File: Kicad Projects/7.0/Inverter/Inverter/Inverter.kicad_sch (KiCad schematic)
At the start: 75 parts, among them IC1 1ED3322MC12NXUMA1, IC2 B0505S-2W, IC3 B0505S-2W, IC4 B0505S-2W, IC5 1ED3322MC12NXUMA1, J1 Conn_01x02_Male, J2 Conn_01x07_Male, J3 Conn_01x02_Male, U1 LM7809_TO220, U2 LM7809_TO220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

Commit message: Inverter PCB Done
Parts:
- removed C29: 56uF, Capacitor_THT:CP_Radial_D16.0mm_P7.50mm, symbol Device:C_Polarized
- removed C3, C4: 1000uF, 25V 1000uf:CAP_EEEFK1E102AQ, symbol Device:C_Polarized
- added D10, D11, D9: Blue, LED_SMD:LED_0805_2012Metric_Pad1.15x1.40mm_HandSolder, symbol Device:LED
- added D12, D13: Red, LED_SMD:LED_0805_2012Metric_Pad1.15x1.40mm_HandSolder, symbol Device:LED
- added D14, D15, D16, D17, D18, D19: Green, LED_SMD:LED_0805_2012Metric_Pad1.15x1.40mm_HandSolder, symbol Device:LED
- added J4: Output Selector, Connector_PinSocket_1.27mm:PinSocket_1x03_P1.27mm_Vertical, symbol Connector:Conn_01x03_Pin
- added Q1, Q2: FS8205, 8205a:SOT95P280X145-6N, symbol 8205a:FS8205
- added R11, R12: 1.4, Resistor_SMD:R_0805_2012Metric_Pad1.20x1.40mm_HandSolder, symbol Device:R
- added R13, R14, R15, R16, R17: 22K, Resistor_SMD:R_1206_3216Metric_Pad1.30x1.75mm_HandSolder, symbol Device:R
- added R18, R19, R20, R21, R22, R27: 470, Resistor_SMD:R_0603_1608Metric_Pad0.98x0.95mm_HandSolder, symbol Device:R
- added R23, R26: 3.3k, Resistor_SMD:R_0603_1608Metric_Pad0.98x0.95mm_HandSolder, symbol Device:R
- added R24, R25: 2.2k, Resistor_SMD:R_0603_1608Metric_Pad0.98x0.95mm_HandSolder, symbol Device:R
- R1, R3: value 3.3 -> 2.2
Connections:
- net +BATT: now also R13.1, R16.1
- net -BATT: now also D18.1 (K); no longer R7.2
- net DIG+: now also J4.3 (Pin_3), R21.2, R22.2, R27.1
- net DIG-: now also D10.1 (K), D11.1 (K), D19.1 (K), D9.1 (K), Q1.1, Q1.3, Q2.1, Q2.3
- net DIG5V: now also J4.1 (Pin_1); no longer J2.2 (Pin_2)
- net FLT: now also Q1.4, Q1.6
- net GND1: now also D14.1 (K), R24.2
- net GND2: now also D16.1 (K), R25.2
- net INHS: now also R19.1
- net INLS: now also R18.1
- net RDY: now also Q2.4, Q2.6
- net RST: now also R20.1
- net VAux+: now also J3.2 (Pin_2); no longer J3.1 (Pin_1)
- net VAux-: now also J3.1 (Pin_1); no longer J3.2 (Pin_2)
- net VDrive1: now also R23.2
- net VDrive1Neg: now also D15.1 (K)
- net VDrive2: now also R26.2
- net VDrive2Neg: now also D17.1 (K)
- net at R3.2, U7.4: now also IC5.7 (CLAMP), R12.2
- net at R1.2, U7.6: now also IC1.7 (CLAMP), R11.2
- net at IC5.4 (OUT-): now also R12.1
- net at IC1.4 (OUT-): now also R11.1
- new net: D15.2 (A), R24.1
- new net: D17.2 (A), R25.1
- new net: R13.2, R14.1, R15.1, R16.2, R17.1, R7.2
- new net: J2.2 (Pin_2), J4.2 (Pin_2)
- new net: D13.1 (K), Q2.2, Q2.5
- new net: D12.2 (A), R21.1
- new net: D10.2 (A), R19.2
- new net: D9.2 (A), R18.2
- new net: D12.1 (K), Q1.2, Q1.5
- new net: D13.2 (A), R22.1
- new net: D16.2 (A), R26.1
- new net: D18.2 (A), R14.2, R15.2, R17.2
- new net: D19.2 (A), R27.2
- new net: D11.2 (A), R20.2
- new net: D14.2 (A), R23.1
- no-connect marks 2 -> 0
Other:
- moved on the sheet: R10, R8, R9

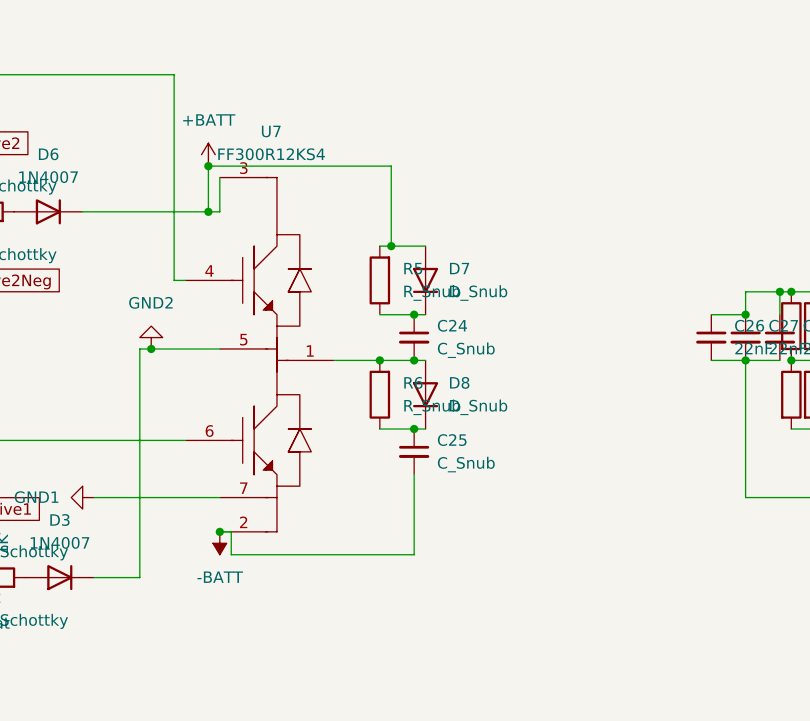
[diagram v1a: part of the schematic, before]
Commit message: IDEK but LTC6804 Ordered
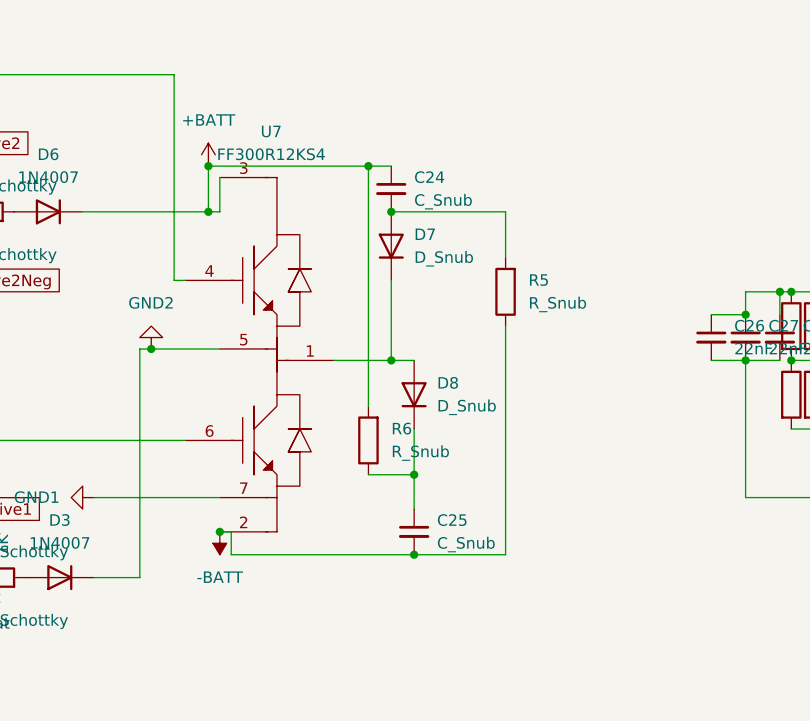
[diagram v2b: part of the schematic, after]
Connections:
- net +BATT: now also C24.1, R6.2; no longer D7.2 (A), R5.2
- net -BATT: now also R5.1
- net at D8.2 (A), U7.1: now also D7.1 (K); no longer C24.2, R6.2
- new net: C24.2, D7.2 (A), R5.2
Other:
- moved on the sheet: C24, C25, D7, D8, R5, R6

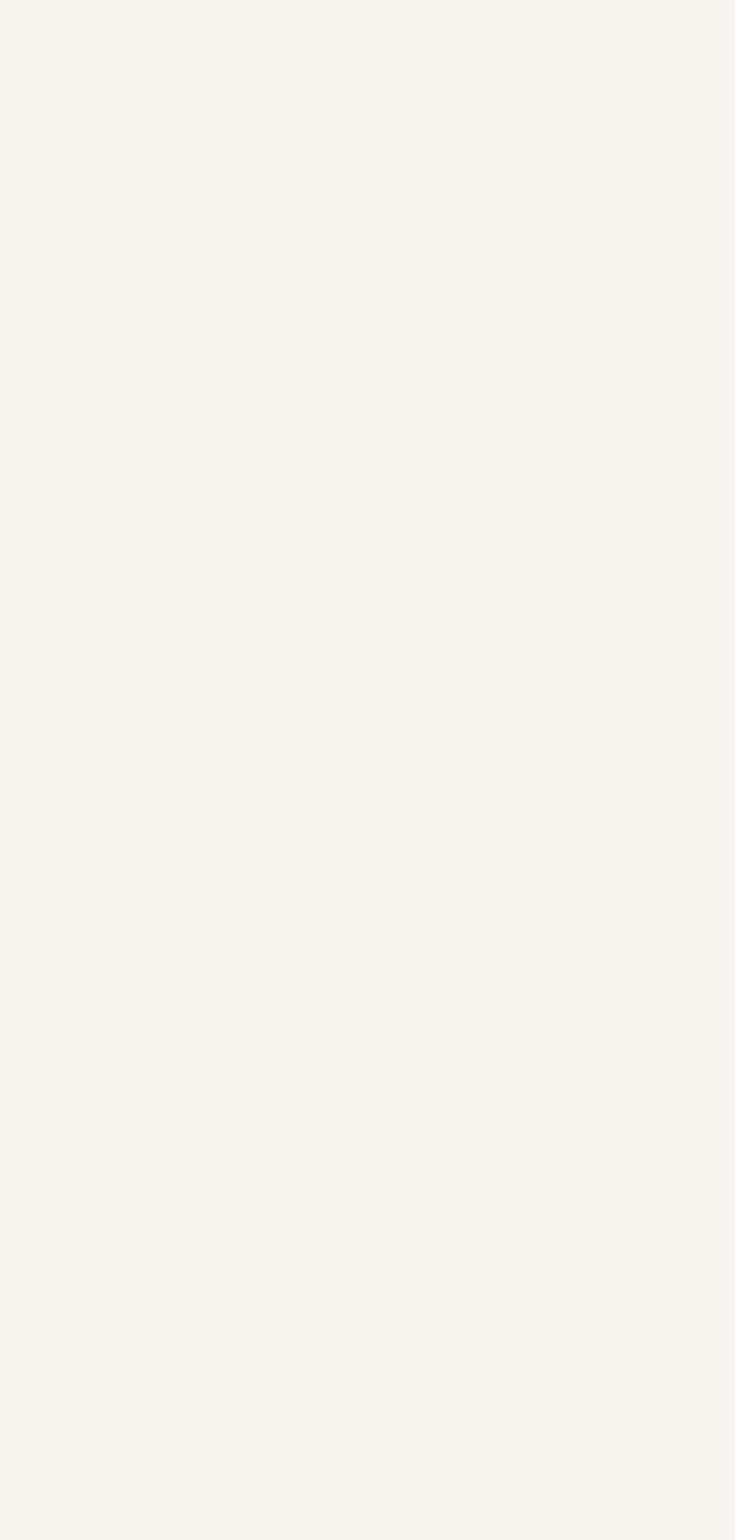
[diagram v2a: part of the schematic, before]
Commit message: Inverter 0 errors ready to export, LU fucked
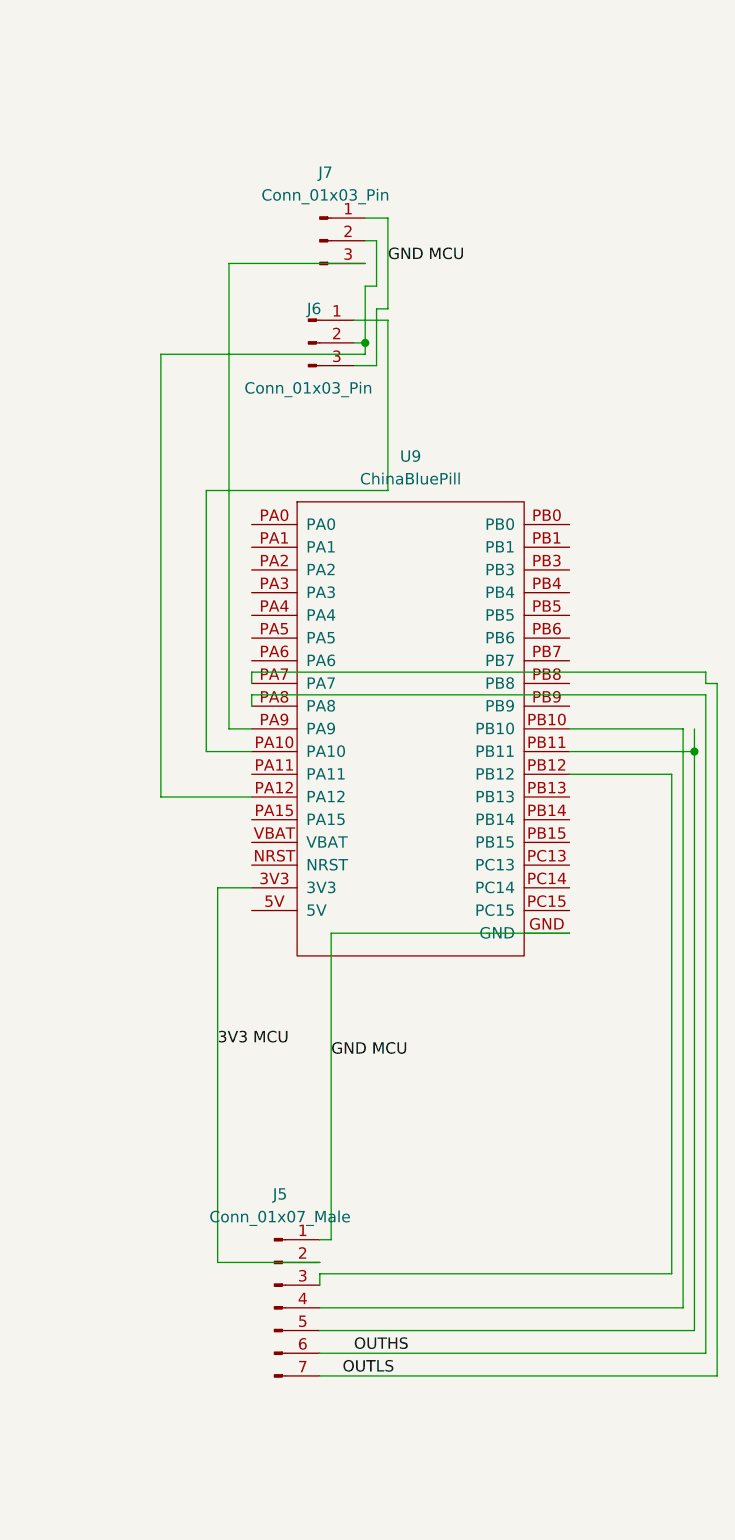
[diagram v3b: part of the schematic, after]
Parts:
- added J5: Conn_01x07_Male, Connector_JST:JST_XH_B7B-XH-A_1x07_P2.50mm_Vertical, symbol Connector:Conn_01x07_Male
- added J6, J7: Conn_01x03_Pin, Connector_JST:JST_XH_S3B-XH-A_1x03_P2.50mm_Horizontal, symbol Connector:Conn_01x03_Pin
- added U9: ChinaBluePill, Blue Pill:ChinaBluePill, symbol Blue Pill:ChinaBluePill
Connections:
- new net: J5.3 (Pin_3), U9.PB12
- new net: J5.4 (Pin_4), U9.PB10
- new net: J5.5 (Pin_5), U9.PB11
- new net: J6.2 (Pin_2), J7.2 (Pin_2), U9.PA12
- new net: J7.3 (Pin_3), U9.PA9
- new net: J6.1 (Pin_1), U9.PA10
- new net 3V3 MCU: J5.2 (Pin_2), U9.3V3
- new net GND MCU: J5.1 (Pin_1), J6.3 (Pin_3), J7.1 (Pin_1), U9.GND
- new net OUTHS: J5.6 (Pin_6), U9.PA8
- new net OUTLS: J5.7 (Pin_7), U9.PA7

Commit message: Inverter gbr generated
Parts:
- removed H1, H2, H3, H4: MountingHole, MountingHole:MountingHole_3.2mm_M3, symbol Mechanical:MountingHole
- added J10, J11, J8: Conn_01x02_Pin, Connector_PinHeader_1.27mm:PinHeader_1x02_P1.27mm_Vertical, symbol Connector:Conn_01x02_Pin
- added J9: NTC, Connector_PinHeader_1.27mm:PinHeader_1x02_P1.27mm_Vertical, symbol Connector:Conn_01x02_Pin
- added R28: NTC Complement, Resistor_SMD:R_0805_2012Metric_Pad1.20x1.40mm_HandSolder, symbol Device:R
- J2, J5: footprint Connector_JST:JST_XH_B7B-XH-A_1x07_P2.50mm_Vertical -> Connector_JST:JST_XH_B8B-XH-A_1x08_P2.50mm_Vertical; symbol Connector:Conn_01x07_Male -> Connector:Conn_01x08_Pin
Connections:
- net DIG+: now also R28.2
- net DIG-: now also J9.2 (Pin_2)
- net at U9.PA0: now also J8.1 (Pin_1)
- net at U9.PA1: now also J5.8 (Pin_8)
- new net: J11.1 (Pin_1), J7.2 (Pin_2)
- new net: J10.1 (Pin_1), J11.2 (Pin_2), J8.2 (Pin_2), U9.PA12
- new net: J2.8 (Pin_8), J9.1 (Pin_1), R28.1
- new net: J10.2 (Pin_2), J6.2 (Pin_2)

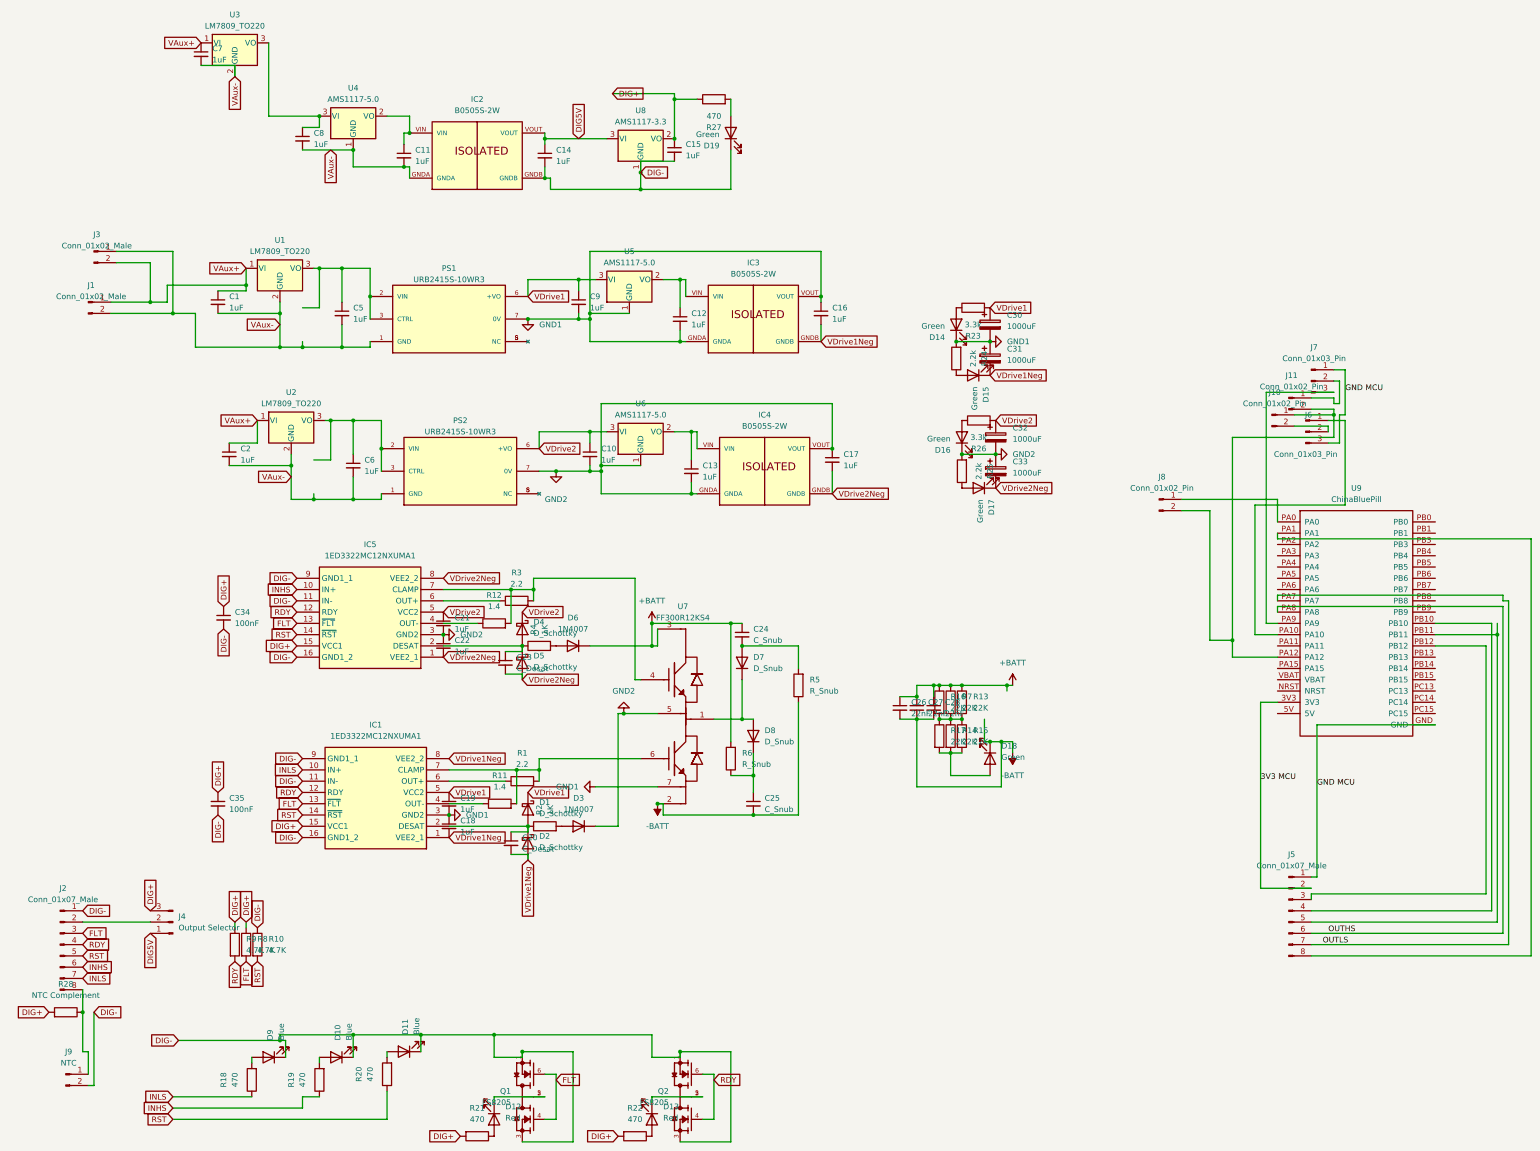
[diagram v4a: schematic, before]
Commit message: Inverter add dc link sense
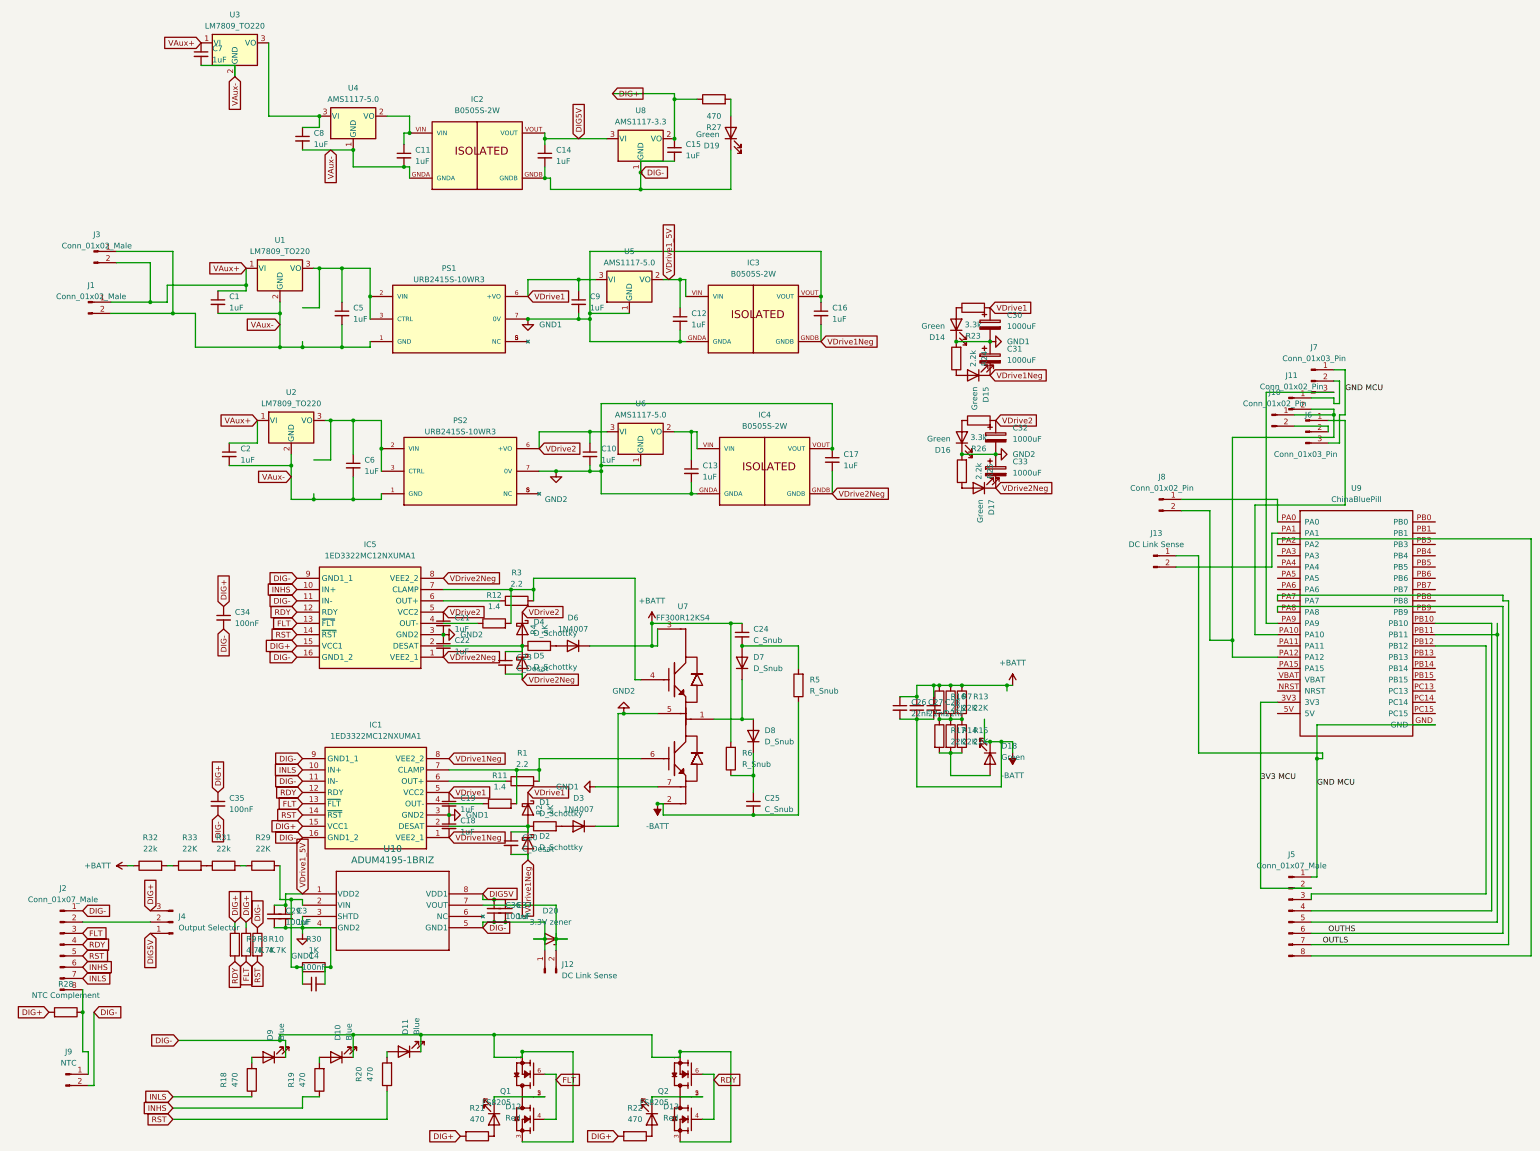
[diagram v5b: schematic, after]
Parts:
- added C29, C36, C4: 100nF, Capacitor_SMD:C_0603_1608Metric_Pad1.08x0.95mm_HandSolder, symbol Device:C_Small
- added C3, C37: 1uF, Capacitor_SMD:C_1206_3216Metric_Pad1.33x1.80mm_HandSolder, symbol Device:C_Small
- added D20: 3.3V zener, Diode_SMD:D_MicroMELF_Handsoldering, symbol Device:D_Zener
- added J12, J13: DC Link Sense, Connector_PinHeader_2.54mm:PinHeader_1x02_P2.54mm_Vertical, symbol Connector:Conn_01x02_Pin
- added R29, R33: 22K, Resistor_SMD:R_0805_2012Metric_Pad1.20x1.40mm_HandSolder, symbol Device:R
- added R30: 1K, Resistor_SMD:R_0805_2012Metric_Pad1.20x1.40mm_HandSolder, symbol Device:R
- added R31, R32: 22k, Resistor_SMD:R_0805_2012Metric_Pad1.20x1.40mm_HandSolder, symbol Device:R
- added U10: ADUM4195-1BRIZ, ADUM4195-1:RI-8-1_ADI, symbol ADUM4195-1:ADUM4195-1BRIZ
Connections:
- net +BATT: now also R32.1
- net DIG-: now also C36.1, C37.2, D20.2 (A), J12.1 (Pin_1), U10.5 (GND1)
- net DIG5V: now also C36.2, C37.1, U10.8 (VDD1)
- net GND MCU: now also J13.1 (Pin_1)
- net GND1: now also C29.1, C3.2, C4.2, R30.2, U10.3 (SHTD), U10.4 (GND2)
- net at J5.8 (Pin_8): now also U9.PA2; no longer U9.PA1
- net VDrive1_5V: now reaches C12.1, IC3.VIN, U5.2 (VO)
- net VDrive1_5V: now also C29.2, C3.1, U10.1 (VDD2)
- new net: R32.2, R33.1
- new net: R31.1, R33.2
- new net: R29.1, R31.2
- new net: C4.1, R29.2, R30.1, U10.2 (VIN)
- new net: D20.1 (K), J12.2 (Pin_2), U10.7 (VOUT)
- new net: J13.2 (Pin_2), U9.PA1
